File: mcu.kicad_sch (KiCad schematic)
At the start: 6 parts, among them U1 PIC32MX795F512L-80x-PF

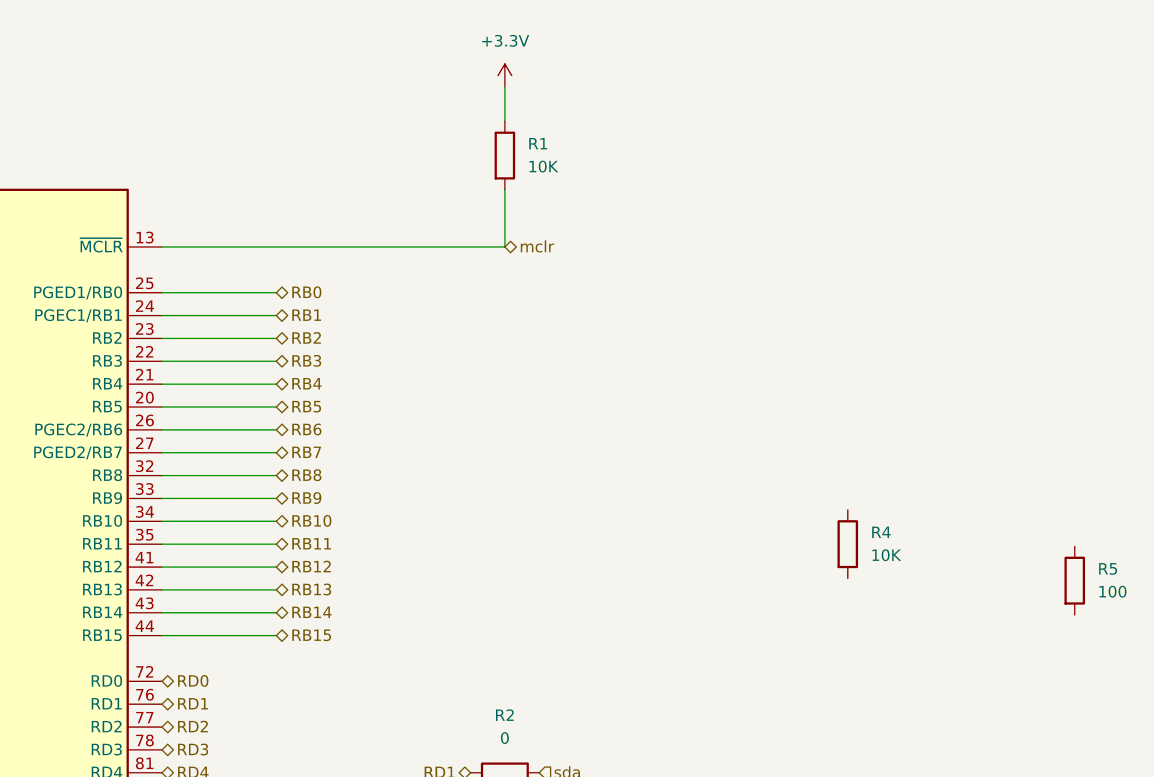
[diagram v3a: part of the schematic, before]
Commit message: feat: add orphaned PCB components to schematics - R4/R5 MCU, R41/R42 OLED, C37/C38 power
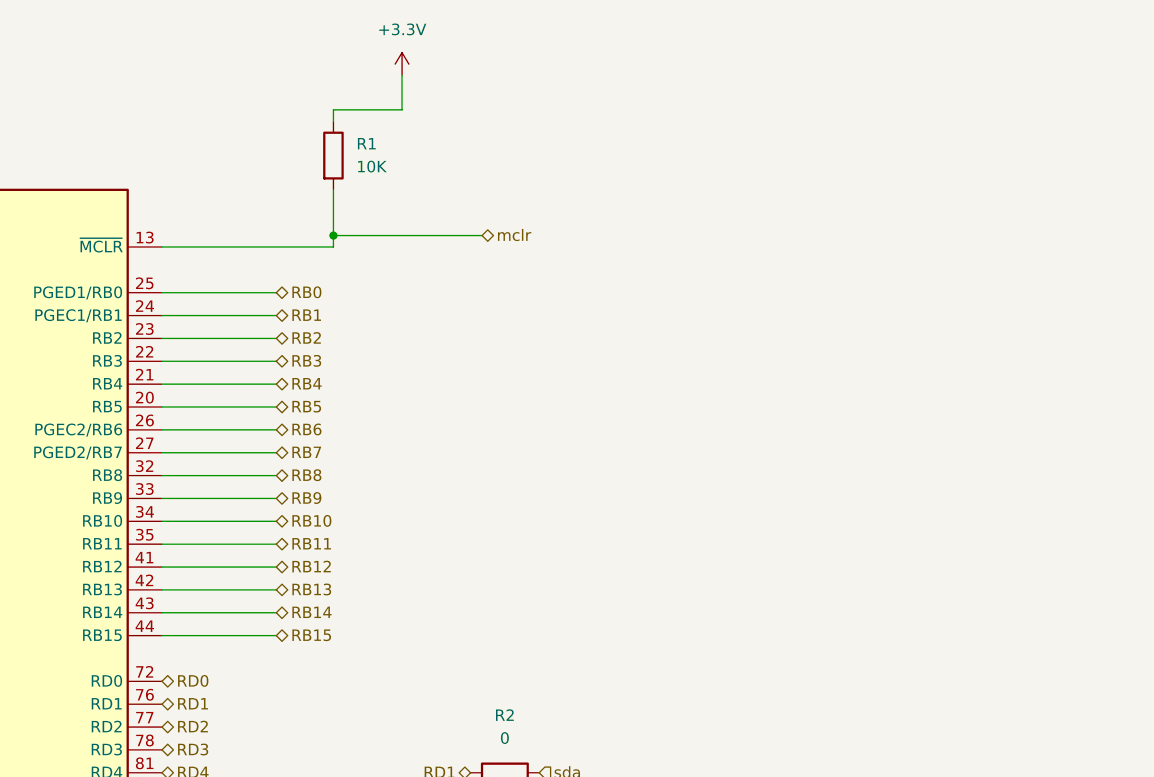
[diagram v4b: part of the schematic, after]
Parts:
- removed R4: 10K, Resistor_SMD:R_0805_2012Metric, symbol Device:R
- removed R5: 100, Resistor_SMD:R_0805_2012Metric, symbol Device:R
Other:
- moved on the sheet: R1
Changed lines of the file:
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@@
+	)
+	(junction
+		(at 184.15 36.83)
+		(diameter 0)
+		(color 0 0 0 0)
 	)
 	(junction
@@
 	(wire
 		(pts
-			(xy 203.2 31.75) (xy 203.2 38.1)
+			(xy 191.77 22.86) (xy 191.77 19.05)
 		)
 		(stroke
@@
 	(wire
 		(pts
-			(xy 203.2 20.32) (xy 203.2 24.13)
+			(xy 184.15 22.86) (xy 184.15 24.13)
 		)
 		(stroke
@@
 	(wire
 		(pts
+			(xy 184.15 22.86) (xy 191.77 22.86)
+		)
+		(stroke
+			(width 0)
+			(type default)
+		)
+	)
+	(wire
+		(pts
 			(xy 177.8 48.26) (xy 165.1 48.26)
 		)
@@
 	(wire
 		(pts
+			(xy 184.15 36.83) (xy 184.15 31.75)
+		)
+		(stroke
+			(width 0)
+			(type default)
+		)
+	)
+	(wire
+		(pts
 			(xy 124.46 27.94) (xy 127 27.94)
 		)
@@
 	(wire
 		(pts
+			(xy 184.15 36.83) (xy 184.15 38.1)
+		)
+		(stroke
+			(width 0)
+			(type default)
+		)
+	)
+	(wire
+		(pts
 			(xy 177.8 55.88) (xy 165.1 55.88)
 		)
@@
 	(wire
 		(pts
+			(xy 184.15 36.83) (xy 200.66 36.83)
+		)
+		(stroke
+			(width 0)
+			(type default)
+		)
+	)
+	(wire
+		(pts
+			(xy 184.15 38.1) (xy 165.1 38.1)
+		)
+		(stroke
+			(width 0)
+			(type default)
+		)
+	)
+	(wire
+		(pts
 			(xy 121.92 21.59) (xy 121.92 27.94)
 		)
@@
 		(pts
 			(xy 177.8 45.72) (xy 165.1 45.72)
-		)
-		(stroke
-			(width 0)
-			(type default)
-		)
-	)
-	(wire
-		(pts
-			(xy 203.2 38.1) (xy 165.1 38.1)
 		)
 		(stroke
@@
 	(hierarchical_label "mclr"
 		(shape bidirectional)
-		(at 203.2 38.1 0)
+		(at 200.66 36.83 0)
 		(effects
 			(font
@@
 	(symbol
 		(lib_id "Device:R")
-		(at 266.517 75.175 0)
-		(unit 1)
-		(body_style 1)
-		(exclude_from_sim no)
-		(in_bom yes)
-		(on_board yes)
-		(in_pos_files yes)
-		(dnp no)
-		(fields_autoplaced yes)
-		(property "Reference" "R5"
-			(at 269.057 73.905 0)
-			(show_name no)
-			(do_not_autoplace no)
-			(effects
-				(font
-					(size 1.27 1.27)
-				)
-				(justify left)
-			)
-		)
-		(property "Value" "100"
-			(at 269.057 76.445 0)
-			(show_name no)
-			(do_not_autoplace no)
-			(effects
-				(font
-					(size 1.27 1.27)
-				)
-				(justify left)
-			)
-		)
-		(property "Footprint" "Resistor_SMD:R_0805_2012Metric"
-			(at 264.739 75.175 90)
-			(hide yes)
-			(show_name no)
-			(do_not_autoplace no)
-			(effects
-				(font
-					(size 1.27 1.27)
-				)
-			)
-		)
-		(property "Datasheet" ""
-			(at 266.517 75.175 0)
-			(hide yes)
-			(show_name no)
-			(do_not_autoplace no)
-			(effects
-				(font
-					(size 1.27 1.27)
-				)
-			)
-		)
-		(property "Description" ""
-			(at 266.517 75.175 0)
-			(show_name no)
-			(do_not_autoplace no)
-			(effects
-				(font
-					(size 1.27 1.27)
-				)
-			)
-		)
-		(pin "1"
-		)
-		(pin "2"
-		)
-		(instances
-			(project "cnc_pic32"
-				(path "/13dbfc1f-be47-44ca-9042-3d6a9a657d7d/64cf98d4-7353-423c-baad-4e05534717be"
-					(reference "R5")
-					(unit 1)
-				)
-			)
-		)
-	)
-	(symbol
-		(lib_id "Device:R")
 		(at 203.2 96.52 90)
 		(unit 1)
@@
 	)
 	(symbol
-		(lib_id "Device:R")
-		(at 241.3 71.12 0)
-		(unit 1)
-		(body_style 1)
-		(exclude_from_sim no)
-		(in_bom yes)
-		(on_board yes)
-		(in_pos_files yes)
-		(dnp no)
-		(fields_autoplaced yes)
-		(property "Reference" "R4"
-			(at 243.84 69.85 0)
-			(show_name no)
-			(do_not_autoplace no)
-			(effects
-				(font
-					(size 1.27 1.27)
-				)
-				(justify left)
-			)
-		)
-		(property "Value" "10K"
-			(at 243.84 72.39 0)
-			(show_name no)
-			(do_not_autoplace no)
-			(effects
-				(font
-					(size 1.27 1.27)
-				)
-				(justify left)
-			)
-		)
-		(property "Footprint" "Resistor_SMD:R_0805_2012Metric"
-			(at 239.522 71.12 90)
-			(hide yes)
-			(show_name no)
-			(do_not_autoplace no)
-			(effects
-				(font
-					(size 1.27 1.27)
-				)
-			)
-		)
-		(property "Datasheet" ""
-			(at 241.3 71.12 0)
-			(hide yes)
-			(show_name no)
-			(do_not_autoplace no)
-			(effects
-				(font
-					(size 1.27 1.27)
-				)
-			)
-		)
-		(property "Description" ""
-			(at 241.3 71.12 0)
-			(show_name no)
-			(do_not_autoplace no)
-			(effects
-				(font
-					(size 1.27 1.27)
-				)
-			)
-		)
-		(pin "1"
-		)
-		(pin "2"
-		)
-		(instances
-			(project "cnc_pic32"
-				(path "/13dbfc1f-be47-44ca-9042-3d6a9a657d7d/64cf98d4-7353-423c-baad-4e05534717be"
-					(reference "R4")
-					(unit 1)
-				)
-			)
-		)
-	)
-	(symbol
 		(lib_id "power:+3.3V")
-		(at 203.2 20.32 0)
+		(at 191.77 19.05 0)
 		(unit 1)
 		(body_style 1)
@@
 		(fields_autoplaced yes)
 		(property "Reference" "#PWR03"
-			(at 203.2 24.13 0)
+			(at 191.77 22.86 0)
 			(hide yes)
 			(show_name no)
@@
 		)
 		(property "Value" "+3.3V"
-			(at 203.2 15.24 0)
+			(at 191.77 13.97 0)
 			(show_name no)
 			(do_not_autoplace no)
@@
 		)
 		(property "Footprint" ""
-			(at 203.2 20.32 0)
+			(at 191.77 19.05 0)
 			(hide yes)
 			(show_name no)
@@
 		)
 		(property "Datasheet" ""
-			(at 203.2 20.32 0)
+			(at 191.77 19.05 0)
 			(hide yes)
 			(show_name no)
@@
 		)
 		(property "Description" ""
-			(at 203.2 20.32 0)
+			(at 191.77 19.05 0)
 			(show_name no)
 			(do_not_autoplace no)
@@
 	(symbol
 		(lib_id "Device:R")
-		(at 203.2 27.94 0)
+		(at 184.15 27.94 0)
 		(unit 1)
 		(body_style 1)
@@
 		(fields_autoplaced yes)
 		(property "Reference" "R1"
-			(at 205.74 26.67 0)
+			(at 186.69 26.67 0)
 			(show_name no)
 			(do_not_autoplace no)
@@
 		)
 		(property "Value" "10K"
-			(at 205.74 29.21 0)
+			(at 186.69 29.21 0)
 			(show_name no)
 			(do_not_autoplace no)
@@
 		)
 		(property "Footprint" "Resistor_SMD:R_0805_2012Metric"
-			(at 201.422 27.94 90)
+			(at 182.372 27.94 90)
 			(hide yes)
 			(show_name no)
@@
 		)
 		(property "Datasheet" ""
-			(at 203.2 27.94 0)
+			(at 184.15 27.94 0)
 			(hide yes)
 			(show_name no)
@@
 		)
 		(property "Description" ""
-			(at 203.2 27.94 0)
-			(show_name no)
-			(do_not_autoplace no)
+			(at 184.15 27.94 0)
+			(show_name no)
+			(do_not_autoplace no)

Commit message: feat: 2-layer stackup, bus net class and schematic cleanup
PCB / project
- Reduce board from 4 layers to 2 (F.Cu / B.Cu) for cheaper fabrication
- Add "bus" net class and reorder net class priorities (bus 0, usb_differential 1, ...)

Schematics
- usb_conector_Ft232: add D+ / D-- labels on the USB mini-B data pair
- ft232: add 10K pull-ups, 100nf decoupling and test points on +3.3VA
- tp_ft232: remove solder jumpers JP1/JP2 (TX_Rpi / RX_Rpi now direct)
- Usb_pic32: add C38 100nf decoupling on +5V
- oled: expand connector J25 from 7 to 8 pins
- mcu / idc / power / zigbee / buttons / cnc_pic32: annotation and net cleanup

docs
- Add USB-Mini-B pinout reference images
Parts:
- removed R2, R3: 0, Resistor_SMD:R_0805_2012Metric, symbol Device:R
- added C11: 100nf, Capacitor_SMD:C_0805_2012Metric, symbol Device:C
- added C12, C13: 15p, Capacitor_SMD:C_0805_2012Metric, symbol Device:C
- added J1: icd, Connector_PinHeader_2.54mm:PinHeader_1x06_P2.54mm_Horizontal, symbol Connector:Conn_01x06_Pin
- added JP3: sda_jp, symbol Jumper:Jumper_2_Bridged
- added JP4: scl_jp, symbol Jumper:Jumper_2_Bridged
- added JP5: pgc1, Jumper:SolderJumper-2_P1.3mm_Open_RoundedPad1.0x1.5mm, symbol Jumper:Jumper_2_Bridged
- added JP6: pgd1, Jumper:SolderJumper-2_P1.3mm_Open_RoundedPad1.0x1.5mm, symbol Jumper:Jumper_2_Bridged
- added JP7: pgc2, Jumper:SolderJumper-2_P1.3mm_Bridged_RoundedPad1.0x1.5mm, symbol Jumper:Jumper_2_Bridged
- added JP8: pgd2, Jumper:SolderJumper-2_P1.3mm_Bridged_RoundedPad1.0x1.5mm, symbol Jumper:Jumper_2_Bridged
- added R6: 1K, Resistor_SMD:R_0805_2012Metric, symbol Device:R
- added R7: 1M, Resistor_SMD:R_0805_2012Metric, symbol Device:R
- added Y1: 8MHZ, Crystal:Crystal_SMD_0603-4Pin_6.0x3.5mm, symbol Device:Crystal_GND24
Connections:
- net +3.3V: now also C11.1, J1.2 (Pin_2)
- net GND: now also C11.2, C12.2, C13.2, J1.3 (Pin_3), Y1.2, Y1.4
- net OSC1: now also C13.1, R7.2, Y1.3
- net OSC2: now also R6.1
- net RB0: now also JP5.1 (A)
- net RB1: now also JP6.1 (A)
- net RB4: now also J1.6 (Pin_6)
- net RB6: now also J1.5 (Pin_5), JP5.2 (B), JP7.1 (A), JP7.2 (B)
- net RB7: now also J1.4 (Pin_4), JP6.2 (B), JP8.1 (A), JP8.2 (B)
- net RD0: now also JP3.1 (A)
- net RD1: now also JP4.1 (A)
- net mclr: now also J1.1 (Pin_1)
- net scl: now also JP4.2 (B)
- net sda: now also JP3.2 (B)
- new net: C12.1, R6.2, R7.1, Y1.1
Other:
- removed sheet buttons
- note added: "PGEC1 K1 PGEC1/AN1/CN3/RB1 PGED1 K2 PGED1/AN0/CN2/RB0 PGEC2 J3 (ver nota) PGEC2/.../RB6 PGED2 J3 PGED2/AN7/RB7 MCLR F1 MCLR"
- moved on the sheet: R1, U1

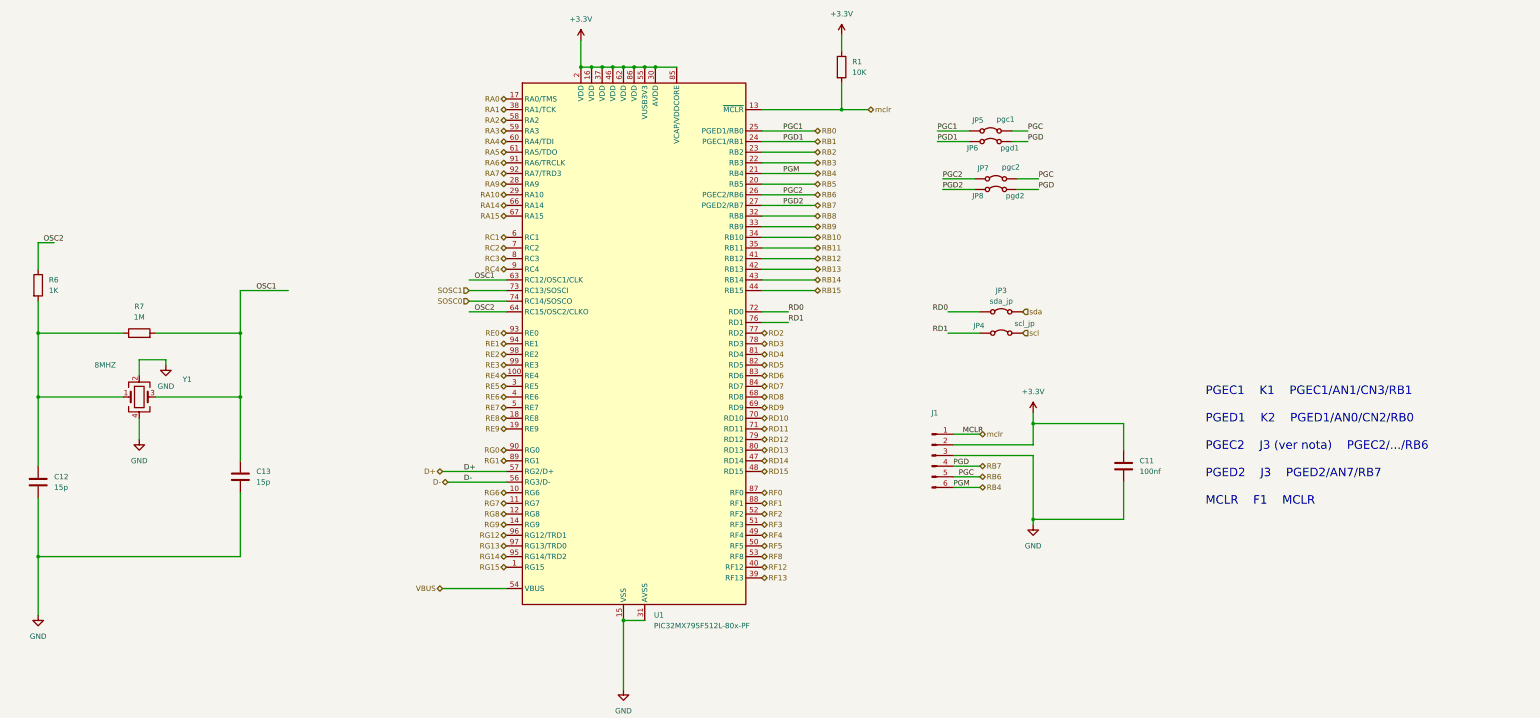
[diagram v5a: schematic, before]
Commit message: feat: add MA240011 module sheet with labeled pins + Altium socket footprint
Esquemático
- Nueva hoja hija MA240011.kicad_sch (módulo PIC32 TQFP-100) referenciada
  desde la hoja MA240011 de mcu.kicad_sch
- mcu.kicad_sch: los 83 pines jerárquicos de MA240011 quedan rotulados con un
  label local del mismo nombre; 81 de ellos con un tramo de wire de 2.54 mm
  (un label solo no conecta a un pin de hoja) y RD4/RD5 sobre el wire existente
- mcu.kicad_sch: borde derecho del sheet 104.775 -> 106.68 mm y sus 41 pines,
  para quedar en grilla de 1.27 mm (evita 41 avisos endpoint_off_grid)
- ERC: 341 -> 158 violaciones; pin_not_connected 120 -> 39,
  isolated_pin_label 113 -> 10, endpoint_off_grid 6 -> 6
- power / zigbee / oled / pololu / cnc_pic32: pines MS1-MS3, conectores y
  anotacion de netnames

PCB
- Referencia de los 132 footprints a size 0.8 x 0.8 mm y thickness 0.12 mm
  (render_cache obsoleto eliminado para forzar el re-render)

Footprints
- lib/altium.pretty/MA240011_Socket_TQFP100_100pin.kicad_mod: zocalo adaptador
  de 100 pines TH pitch 1.27 mm convertido desde altium/Multimedia/MM20141127.PcbDoc
  (J4, patron MA240011); pads girados 90 grados sentido horario
- fp-lib-table: alta de la biblioteca "altium" (${KIPRJMOD}/lib/altium.pretty)

.gitignore
- Ignorar altium/, tmp/ y *.bkp (backups de KiCad)
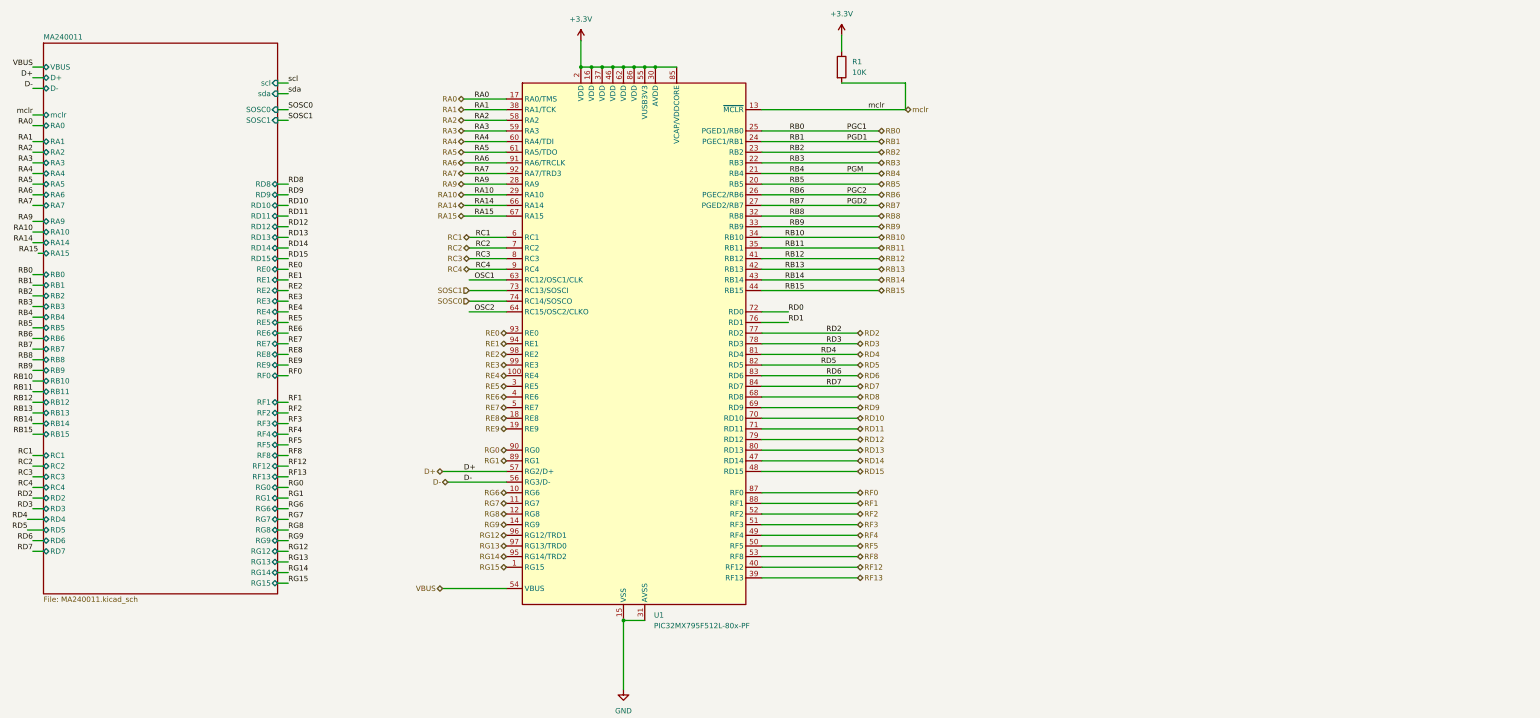
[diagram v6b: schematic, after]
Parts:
- removed C11: 100nf, Capacitor_SMD:C_0805_2012Metric, symbol Device:C
- removed C12, C13: 15p, Capacitor_SMD:C_0805_2012Metric, symbol Device:C
- removed J1: icd, Connector_PinHeader_2.54mm:PinHeader_1x06_P2.54mm_Horizontal, symbol Connector:Conn_01x06_Pin
- removed JP3: sda_jp, symbol Jumper:Jumper_2_Bridged
- removed JP4: scl_jp, symbol Jumper:Jumper_2_Bridged
- removed JP5: pgc1, Jumper:SolderJumper-2_P1.3mm_Open_RoundedPad1.0x1.5mm, symbol Jumper:Jumper_2_Bridged
- removed JP6: pgd1, Jumper:SolderJumper-2_P1.3mm_Open_RoundedPad1.0x1.5mm, symbol Jumper:Jumper_2_Bridged
- removed JP7: pgc2, Jumper:SolderJumper-2_P1.3mm_Bridged_RoundedPad1.0x1.5mm, symbol Jumper:Jumper_2_Bridged
- removed JP8: pgd2, Jumper:SolderJumper-2_P1.3mm_Bridged_RoundedPad1.0x1.5mm, symbol Jumper:Jumper_2_Bridged
- removed R6: 1K, Resistor_SMD:R_0805_2012Metric, symbol Device:R
- removed R7: 1M, Resistor_SMD:R_0805_2012Metric, symbol Device:R
- removed Y1: 8MHZ, Crystal:Crystal_SMD_0603-4Pin_6.0x3.5mm, symbol Device:Crystal_GND24
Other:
- added sheet MA240011 (MA240011.kicad_sch)
- note removed: "PGEC1 K1 PGEC1/AN1/CN3/RB1 PGED1 K2 PGED1/AN0/CN2/RB0 PGEC2 J3 (ver nota) PGEC2/.../RB6 PGED2 J3 PGED2/AN7/RB7 MCLR F1 MCLR"

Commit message: add files
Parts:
- added R43: 0, Resistor_SMD:R_0805_2012Metric, symbol Device:R
- U1: LCSC (none) -> C638480
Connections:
- net +3.3V: no longer U1.85 (VCAP/VDDCORE)
- net VBUS: now also R43.2; no longer U1.54 (VBUS)
- new net: R43.1, U1.54 (VBUS)
- new net VCAP_VDD_CORE: U1.85 (VCAP/VDDCORE)
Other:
- moved on the sheet: R1, U1

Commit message: updated
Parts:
- R43: footprint Resistor_SMD:R_0805_2012Metric -> Resistor_SMD:R_0603_1608Metric
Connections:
- net RC4 renamed RC4_SDI1
- net RD0 renamed RD0_SDO1
- net RD10 renamed RD10_SCK1
- net RD14 renamed RD14_SS3
- net RD15 renamed RD15_SCK3
- net RF12 renamed RF12_SS4
- net RF13 renamed RF13_SCK4
- net RF2 renamed RF2_SDI3
- net RF3 renamed RF3_USBID
- net RF4 renamed RF4_SDO4
- net RF5 renamed RF5_SDI4
- net RF8 renamed RF8_SDO3
- net RG7 renamed RG7_U3RX
- net RG8 renamed RG8_U3TX
- no-connect marks 0 -> 1
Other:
- sheet MA240011 ports: added RD14_SS3_U4RX, RF12_SS4, RF13_SCK4, RF4_SDO4, RF5_SDI4; removed RD14, RF12, RF13, RF4, RF5
